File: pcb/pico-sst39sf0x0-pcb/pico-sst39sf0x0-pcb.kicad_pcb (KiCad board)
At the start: 2 copper layers, 101.6 x 54.6 mm, 52 parts, among them Q1 BSS138, Q10 BSS138, Q11 BSS138, Q12 BSS138, Q13 BSS138, Q14 BSS138, Q15 BSS138, Q16 BSS138, Q17 BSS138, Q18 BSS138, Q19 BSS138, Q2 BSS138, Q20 BSS138, Q21 BSS138, Q22 BSS138, Q23 BSS138, Q24 BSS138, Q3 BSS138, Q4 BSS138, Q5 BSS138, Q6 BSS138, Q7 BSS138, Q8 BSS138, Q9 BSS138, SW1 SW_Push, U1 74HC573, U2 SST39SF040, U3 74HC573, U4 Pico, U5 74HC573

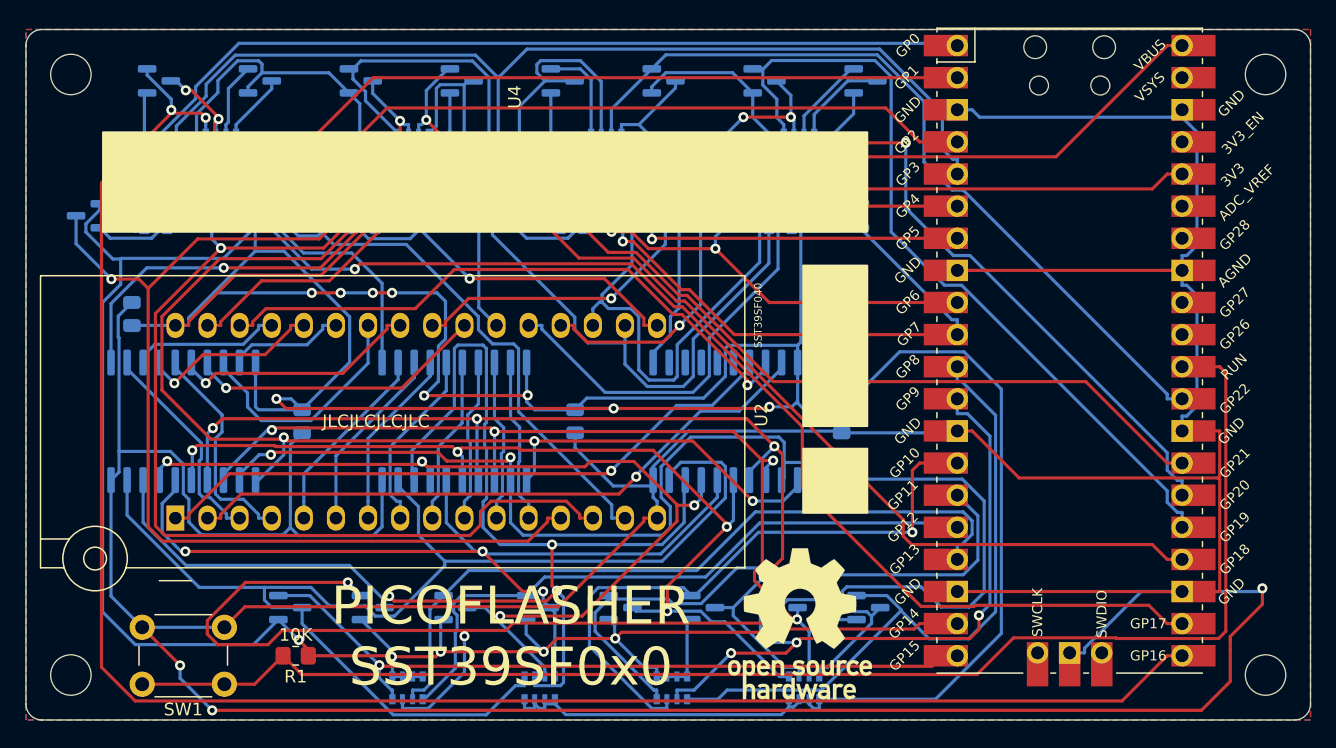
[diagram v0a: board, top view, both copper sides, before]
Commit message: Pcbrev1 (#1)
* Adding LEDs and putting 10k resistor on backside

* Adding polarity protection diode and 10k resistor on backside. Adding LEDS on front side

* Adding LEDs

* Adding LEDs to the firmware
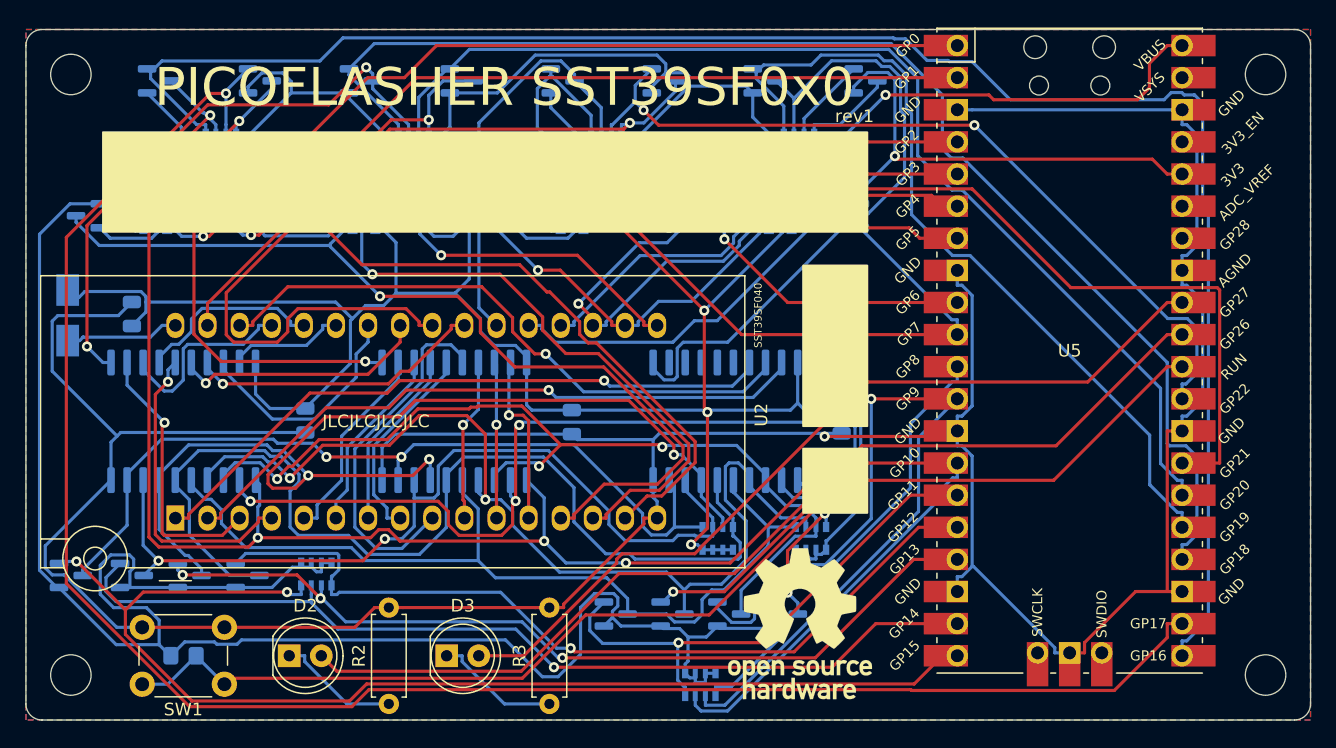
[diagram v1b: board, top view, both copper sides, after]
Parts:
- added D1: M7, Diode_SMD:D_SMA, B.Cu at (17.3, 58.2)
- added D2: LED, LED_THT:LED_D5.0mm, F.Cu at (34.8, 85.1)
- added D3: LED, LED_THT:LED_D5.0mm, F.Cu at (47.2, 85.1)
- added R2: R, Resistor_THT:R_Axial_DIN0207_L6.3mm_D2.5mm_P7.62mm_Horizontal, F.Cu at (42.7, 88.9)
- added R3: R, Resistor_THT:R_Axial_DIN0207_L6.3mm_D2.5mm_P7.62mm_Horizontal, F.Cu at (55.4, 88.9)
- C1, C2, C3, C4: footprint Resistor_SMD:R_0805_2012Metric -> Capacitor_SMD:C_0805_2012Metric
- R1: moved to B.Cu
- moved Q7 23.1 mm to (31.5, 78.7)
- moved Q8 21.2 mm to (26.9, 78.7)
- moved Q9 19.2 mm to (22.4, 78.7)
- moved RN6 18.4 mm to (68.7, 75.8)
- moved Q10 17.5 mm to (17.5, 78.7)
- moved RN3 11.8 mm to (76.1, 75.8)
- moved RN4 11.5 mm to (36.9, 78.6)
- moved R1 8.87 mm to (26.4, 85.1), turned to 0 degrees
- moved Q1 6.53 mm to (74.1, 81.8)
- moved Q2 4.50 mm to (69.6, 81.8)
- moved Q3 2.48 mm to (65.1, 81.8)
- moved RN1 2.26 mm to (67.3, 87.4)
- moved Q4 0.63 mm to (60.6, 81.8)
- moved C3 0.26 mm to (57.1, 66.6)
- moved C2 0.26 mm to (36.1, 66.5)
- renumbered U5 to U4, U4 to U5
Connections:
- U2 pad 32: +5V -> Net-(D1-Pad1)
- U5 pad 31: unconnected-(U4-Pad31) -> GPIO26_3v3
- U5 pad 32: unconnected-(U4-Pad32) -> GPIO27_3v3
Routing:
- net +5V: track 378.2 -> 258.6 mm, vias 12 -> 5
- net GND: track 387.2 -> 267.9 mm, vias 3 -> 1
- net GPIO26_3v3: track 0.00 -> 79.6 mm
- net GPIO27_3v3: track 0.00 -> 67.4 mm
- net LALS: track 103.4 -> 146.3 mm
- net +3V3: track 340.1 -> 378.9 mm, vias 9 -> 1
- net P6: track 103.8 -> 69.1 mm, vias 3 -> 2
- net P7: track 101.1 -> 66.8 mm, vias 0 -> 2
- net LP7: track 59.5 -> 93.6 mm, vias 1 -> 2
- net ~{OE}: track 38.4 -> 66.7 mm
- net P0: track 108.7 -> 84.1 mm, vias 2 -> 5
- net LD3: track 93.1 -> 68.6 mm, vias 0 -> 1
- net AUS: track 30.9 -> 51.7 mm, vias 2 -> 0
- net RUN: track 112.8 -> 94.5 mm
- net LP0: track 54.0 -> 37.2 mm
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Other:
- board text added: "rev1"

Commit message: Initial commit revision 2
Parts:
- R2, R3: value R -> 560; footprint Resistor_THT:R_Axial_DIN0207_L6.3mm_D2.5mm_P7.62mm_Horizontal -> Resistor_SMD:R_0805_2012Metric_Pad1.20x1.40mm_HandSolder; moved to B.Cu
- moved R3 7.88 mm to (55.5, 81.0), turned to 0 degrees
- moved R2 2.67 mm to (42.7, 86.2)
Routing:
- net GND: track 267.9 -> 284.6 mm, vias 1 -> 3
- net Net-(D3-K): track 9.98 -> 11.8 mm, vias 0 -> 1
- net P3: track 70.5 -> 71.2 mm
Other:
- board text added: "rev2"
- board text removed: "rev1"
